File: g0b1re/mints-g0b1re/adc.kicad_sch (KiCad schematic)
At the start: 45 parts, among them U3 MCP3564R, U6 LM4040CIM3-2.0/NOPB

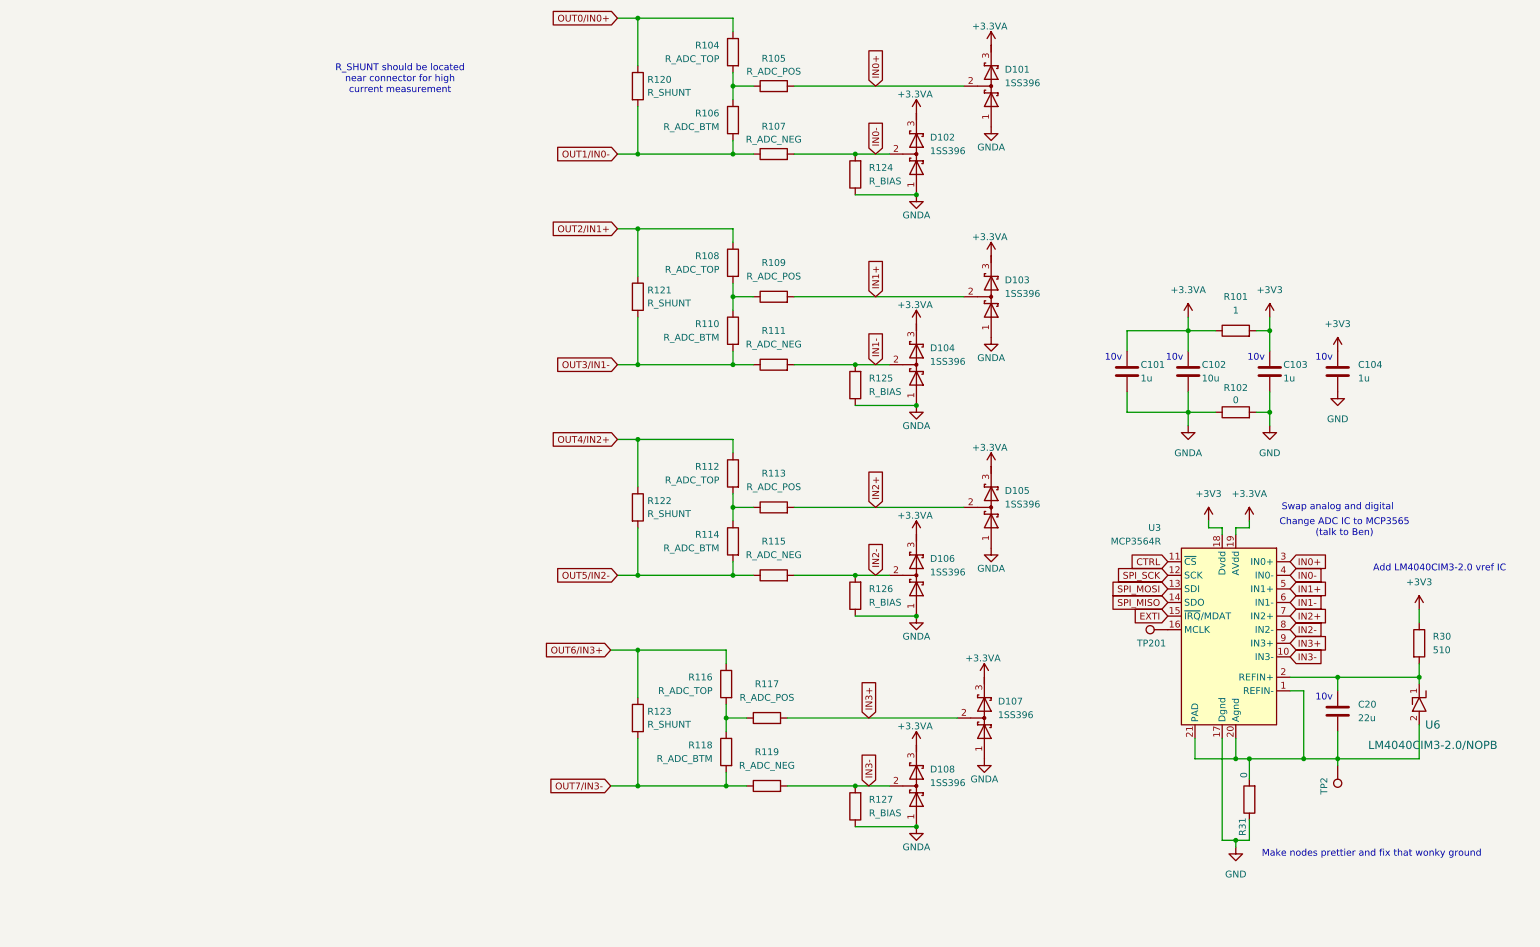
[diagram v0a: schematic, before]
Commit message: polishing schematic, add variants, fix some small issues
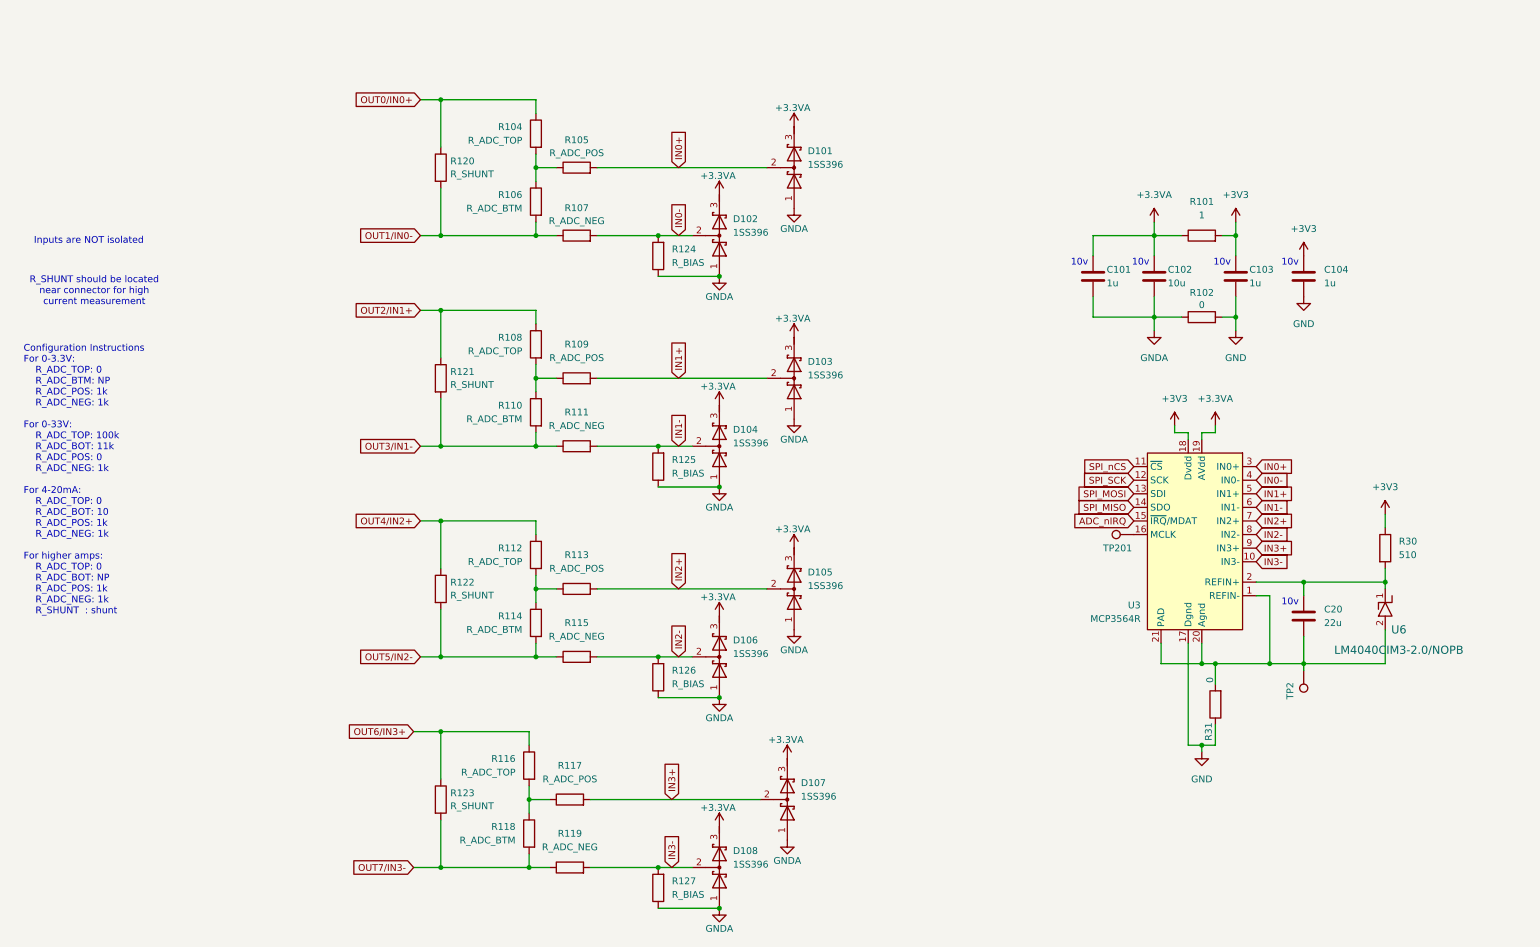
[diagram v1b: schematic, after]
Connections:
- net CTRL renamed SPI_nCS
- net EXTI renamed ADC_nIRQ
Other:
- note added: "Configuration Instructions For 0-3.3V: R_ADC_TOP: 0 R_ADC_BTM: NP R_ADC_POS: 1k R_ADC_NEG: 1k For 0-33V: R_ADC_TOP: 100k R_ADC_BOT: 11k R_ADC_POS: 0 R_ADC_NEG: 1k For 4-20mA: R_ADC_TOP: 0 R_ADC_BOT: 10 R_ADC_POS: 1k R_ADC_NEG: 1k For higher amps: R_ADC_TOP: 0 R_ADC_BOT: NP R_ADC_POS: 1k R_ADC_NEG: 1k R_SHUNT : shunt"
- note added: "Inputs are NOT isolated"
- note removed: "Add LM4040CIM3-2.0 vref IC"
- note removed: "Change ADC IC to MCP3565 (talk to Ben)"
- note removed: "Make nodes prettier and fix that wonky ground"
- note removed: "Swap analog and digital"
- company: (none) -> Portland State Aerospace Society
- title: (none) -> minTS SCADA Board
- moved on the sheet: C101, C102, C103, C104, C20, D101, D102, D103, D104, D105, D106, D107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
